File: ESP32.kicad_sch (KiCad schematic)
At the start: 1 part, among them U1 ESP32-S3

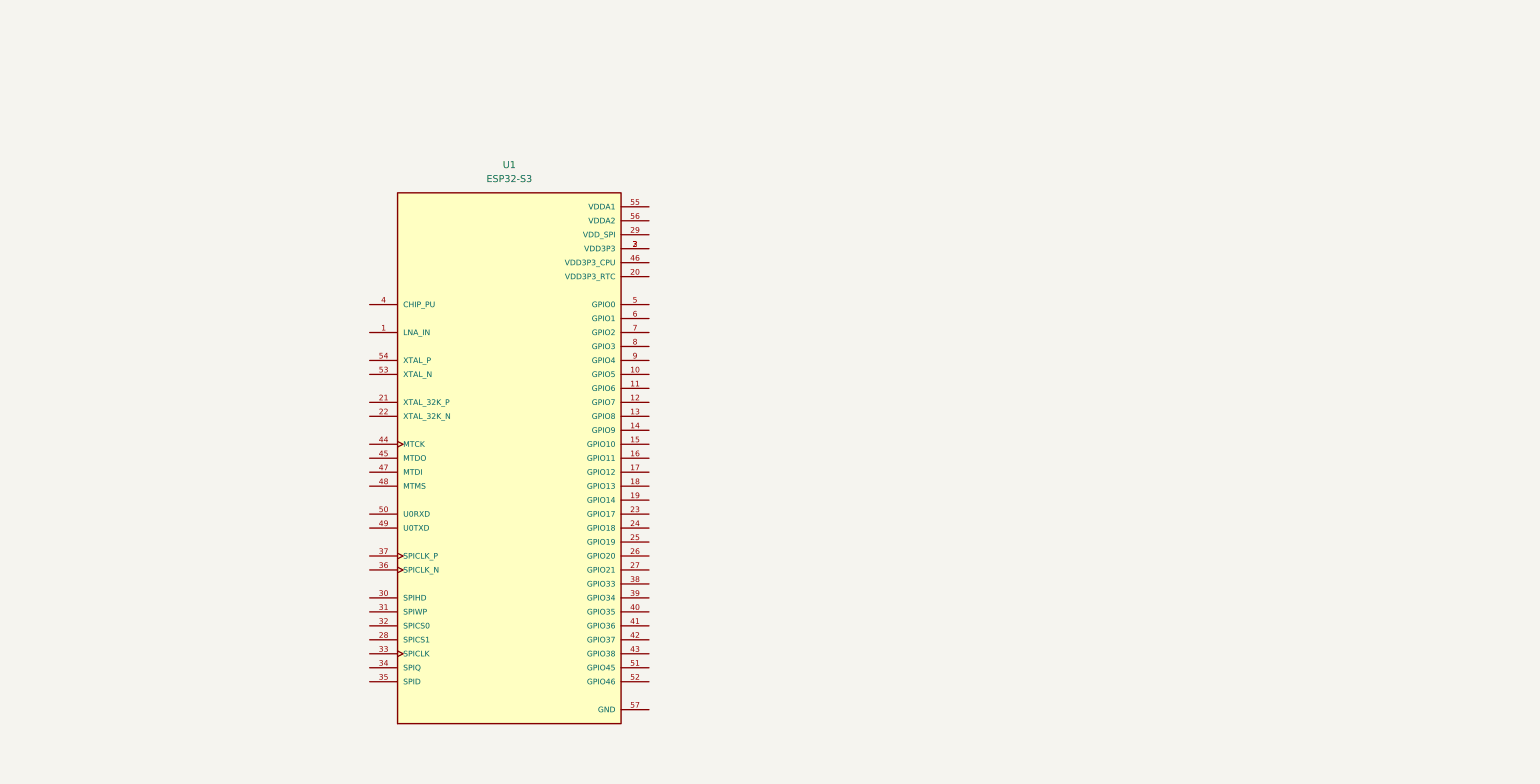
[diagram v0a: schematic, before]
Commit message: FFC camera connector + pin mapping
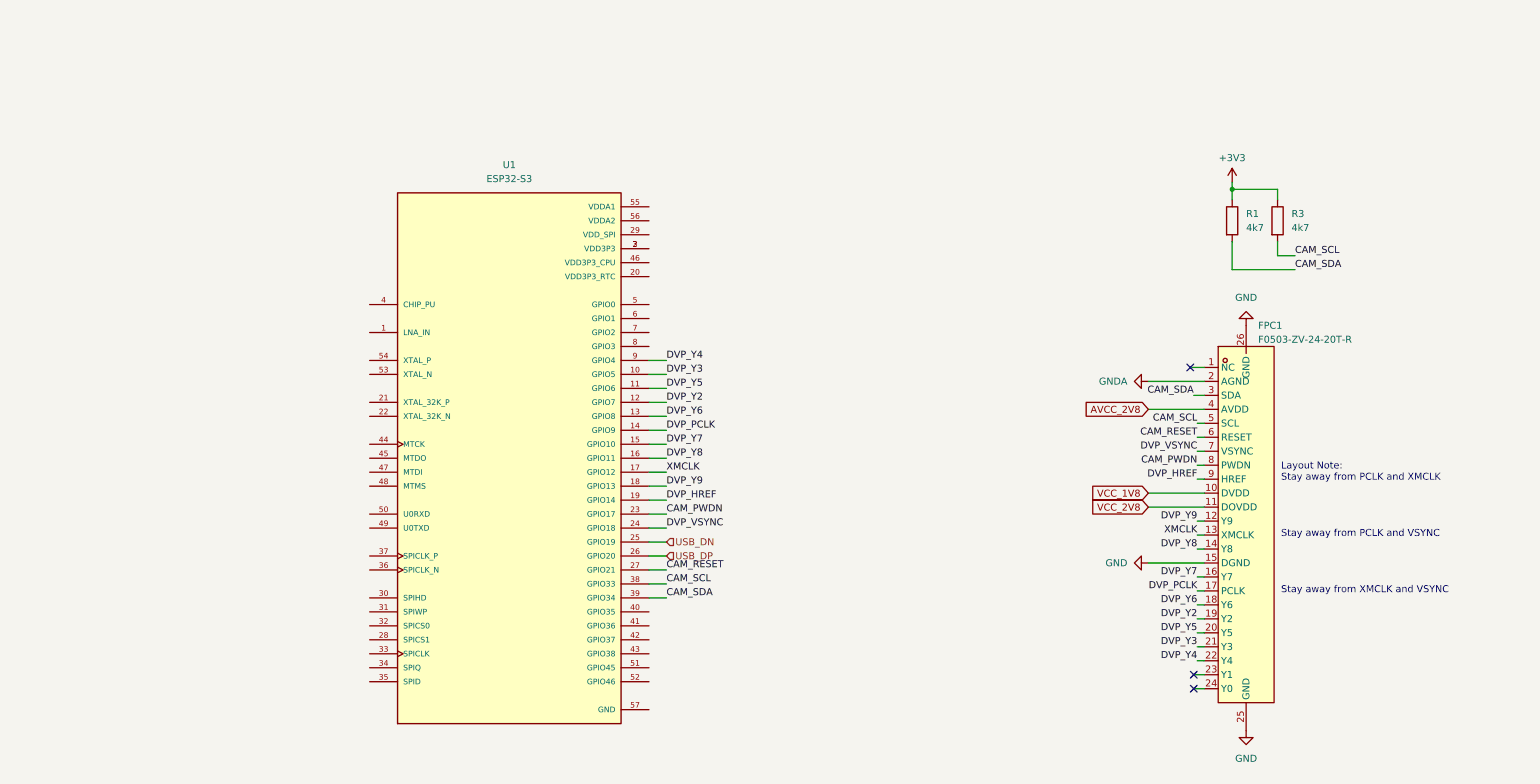
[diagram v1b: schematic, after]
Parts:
- added FPC1: F0503-ZV-24-20T-R, easyeda2kicad:FPC-SMD_F0503-ZV-24-20T-R, symbol easyeda2kicad:F0503-ZV-24-20T-R
- added R1, R3: 4k7, symbol Device:R
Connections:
- net DVP_Y3: now reaches U1.10 (GPIO5)
- net DVP_Y3: now also FPC1.21 (Y3)
- net DVP_Y5: now reaches U1.11 (GPIO6)
- net DVP_Y5: now also FPC1.20 (Y5)
- net DVP_Y2: now reaches U1.12 (GPIO7)
- net DVP_Y2: now also FPC1.19 (Y2)
- net DVP_Y6: now reaches U1.13 (GPIO8)
- net DVP_Y6: now also FPC1.18 (Y6)
- net DVP_PCLK: now reaches U1.14 (GPIO9)
- net DVP_PCLK: now also FPC1.17 (PCLK)
- net DVP_Y7: now reaches U1.15 (GPIO10)
- net DVP_Y7: now also FPC1.16 (Y7)
- net DVP_Y8: now reaches U1.16 (GPIO11)
- net DVP_Y8: now also FPC1.14 (Y8)
- net XMCLK: now reaches U1.17 (GPIO12)
- net XMCLK: now also FPC1.13 (XMCLK)
- net DVP_Y9: now reaches U1.18 (GPIO13)
- net DVP_Y9: now also FPC1.12 (Y9)
- net DVP_HREF: now reaches U1.19 (GPIO14)
- net DVP_HREF: now also FPC1.9 (HREF)
- net CAM_PWDN: now reaches U1.23 (GPIO17)
- net CAM_PWDN: now also FPC1.8 (PWDN)
- net DVP_VSYNC: now reaches U1.24 (GPIO18)
- net DVP_VSYNC: now also FPC1.7 (VSYNC)
- net USB_DN: now reaches U1.25 (GPIO19)
- net USB_DP: now reaches U1.26 (GPIO20)
- net CAM_RESET: now reaches U1.27 (GPIO21)
- net CAM_RESET: now also FPC1.6 (RESET)
- net CAM_SCL: now reaches U1.38 (GPIO33)
- net CAM_SCL: now also FPC1.5 (SCL), R3.2
- net CAM_SDA: now reaches U1.39 (GPIO34)
- net CAM_SDA: now also FPC1.3 (SDA), R1.2
- net DVP_Y4: now reaches U1.9 (GPIO4)
- net DVP_Y4: now also FPC1.22 (Y4)
- new net +3V3: R1.1, R3.1
- new net AVCC_2V8: FPC1.4 (AVDD)
- new net GND: FPC1.15 (DGND), FPC1.25 (GND), FPC1.26 (GND)
- new net GNDA: FPC1.2 (AGND)
- new net VCC_1V8: FPC1.10 (DVDD)
- new net VCC_2V8: FPC1.11 (DOVDD)
- no-connect marks 0 -> 3
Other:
- note added: "Layout Note: Stay away from PCLK and XMCLK Stay away from PCLK and VSYNC Stay away from XMCLK and VSYNC"

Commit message: revving up
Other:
- moved on the sheet: FPC1, R1, U1

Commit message: grow todo but also do a lot of work
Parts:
- added C1 (x5): 10u, Capacitor_SMD:C_0603_1608Metric, symbol Device:C
- added C3 (x7): 100n, Capacitor_SMD:C_0402_1005Metric, symbol Device:C
- added FB1: 100R-800mA, Inductor_SMD:L_0402_1005Metric, symbol Device:FerriteBead_Small
- added L1: 3n9, Inductor_SMD:L_0402_1005Metric, symbol Device:L
- added R9: 1k, Resistor_SMD:R_0402_1005Metric, symbol Device:R
- R1, R3: footprint (none) -> Resistor_SMD:R_0402_1005Metric
- U1: value ESP32-S3 -> ESP32-S3FH4R2; footprint IC_ESP32-S3 -> mylib:ESP32-S3FH4R2
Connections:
- net +3V3: now also U1.20 (VDD3P3_RTC), U1.46 (VDD3P3_CPU), U1.55 (VDDA1), U1.56 (VDDA2), C1.1, C3.1, C3.1, C3.1, C3.1, L1.1; no longer R1.1, R3.1
- net GND: now also C1.2, C1.2, C1.2, C1.2, C3.1, C3.2, C3.2, C3.2, C3.2, C3.2, C3.2
- net GNDA: now also C1.2
- net VCC_2V8: now also R1.1, R3.1, C1.1, FB1.1
- net at U1.2 (VDD3P3), U1.3 (VDD3P3): now also C1.1, C3.1, C3.2, L1.2
- net at U1.29 (VDD_SPI): now also C3.1
- net CHIP_PU: now reaches U1.4 (CHIP_PU)
- net MTCK: now reaches U1.44 (MTCK)
- net MTDO: now reaches U1.45 (MTDO)
- net MTDI: now reaches U1.47 (MTDI)
- net MTMS: now reaches U1.48 (MTMS)
- net at U1.49 (U0TXD): now also R9.2
- net GPIO0: now reaches U1.5 (GPIO0)
- net AVCC_2V8: no longer names the net of FPC1.4 (AVDD)
- net AVCC_2V8: now also C1.1, FB1.2
- net VCC_1V8 renamed VCC_1V2
- net VCC_1V2: now also C1.1
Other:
- note added: "XTAL_32K_P/N can be used GPIO"
- moved on the sheet: FPC1, R1, R3, U1

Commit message: crystals and drivers
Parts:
- added C3 (x2): 20p, Capacitor_SMD:C_0402_1005Metric, symbol Device:C
- added R27, R28: 0, Resistor_SMD:R_0402_1005Metric, symbol Device:R
- added Y2: 40Mhz, Crystal:Crystal_SMD_3225-4Pin_3.2x2.5mm, symbol Device:Crystal_GND24_Small
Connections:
- net at U1.53 (XTAL_N): now also C3.1, Y2.1
- net at U1.54 (XTAL_P): now also R27.2, R28.1
- new net: C3.1, R27.1, Y2.3
- new net: C3.2, C3.2, Y2.2, Y2.4
- new net E_CLK: R28.2

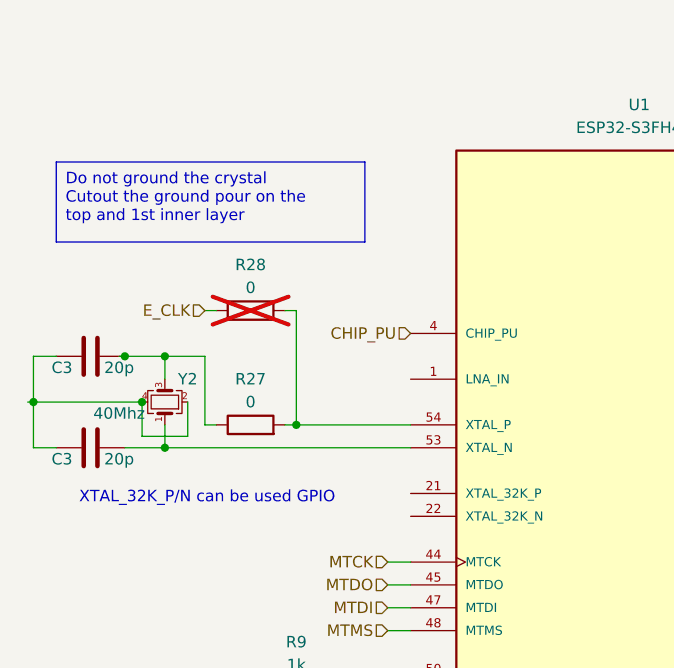
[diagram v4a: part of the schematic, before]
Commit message: more connectors and USB
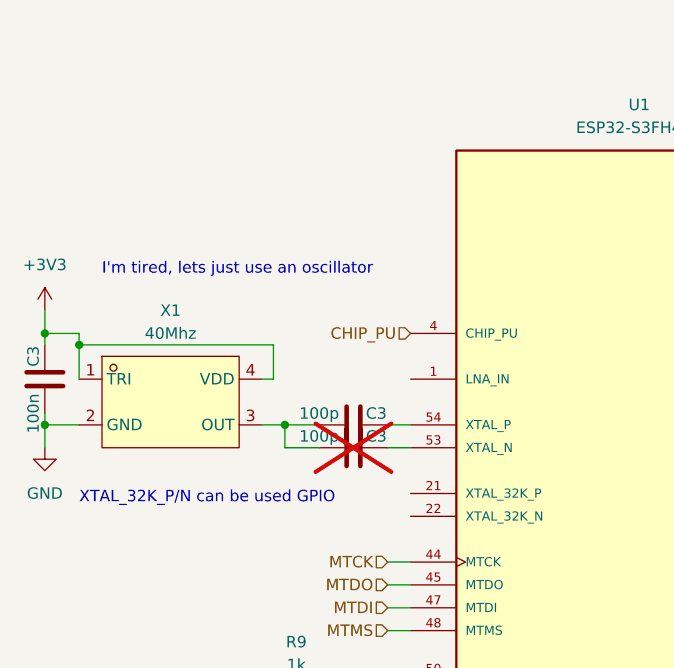
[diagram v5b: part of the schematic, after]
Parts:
- removed C3 (x2): 20p, Capacitor_SMD:C_0402_1005Metric, symbol Device:C
- removed R27, R28: 0, Resistor_SMD:R_0402_1005Metric, symbol Device:R
- removed Y2: 40Mhz, Crystal:Crystal_SMD_3225-4Pin_3.2x2.5mm, symbol Device:Crystal_GND24_Small
- added C3: 100n, Capacitor_SMD:C_0402_1005Metric, symbol Device:C
- added C3 (x2): 100p, Capacitor_SMD:C_0402_1005Metric, symbol Device:C
- added X1: 40Mhz, easyeda2kicad:OSC-SMD_4P-L2.0-W1.6-BL_SIT1602BI, symbol easyeda2kicad:SX1M40.000M10F30TNN
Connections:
- net +3V3: now also C3.2, X1.1 (TRI), X1.4 (VDD)
- net GND: now also C3.1, X1.2 (GND)
- net at U1.54 (XTAL_P): now also C3.2
- net at U1.53 (XTAL_N): now also C3.2
- new net: C3.1, C3.1, X1.3 (OUT)
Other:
- note added: "I'm tired, lets just use an oscillator"
